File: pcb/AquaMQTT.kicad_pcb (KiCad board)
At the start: 2 copper layers, 70 x 65 mm, 22 parts, among them J1 DHW MAIN, J2 DHW HMI, J3 LLC 5V, J4 LLC 3V3, J5 Serial, J6 RTC DS3231, J7 Passthrough, Q1 BC547, Q2 BC547, Q3 BC547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

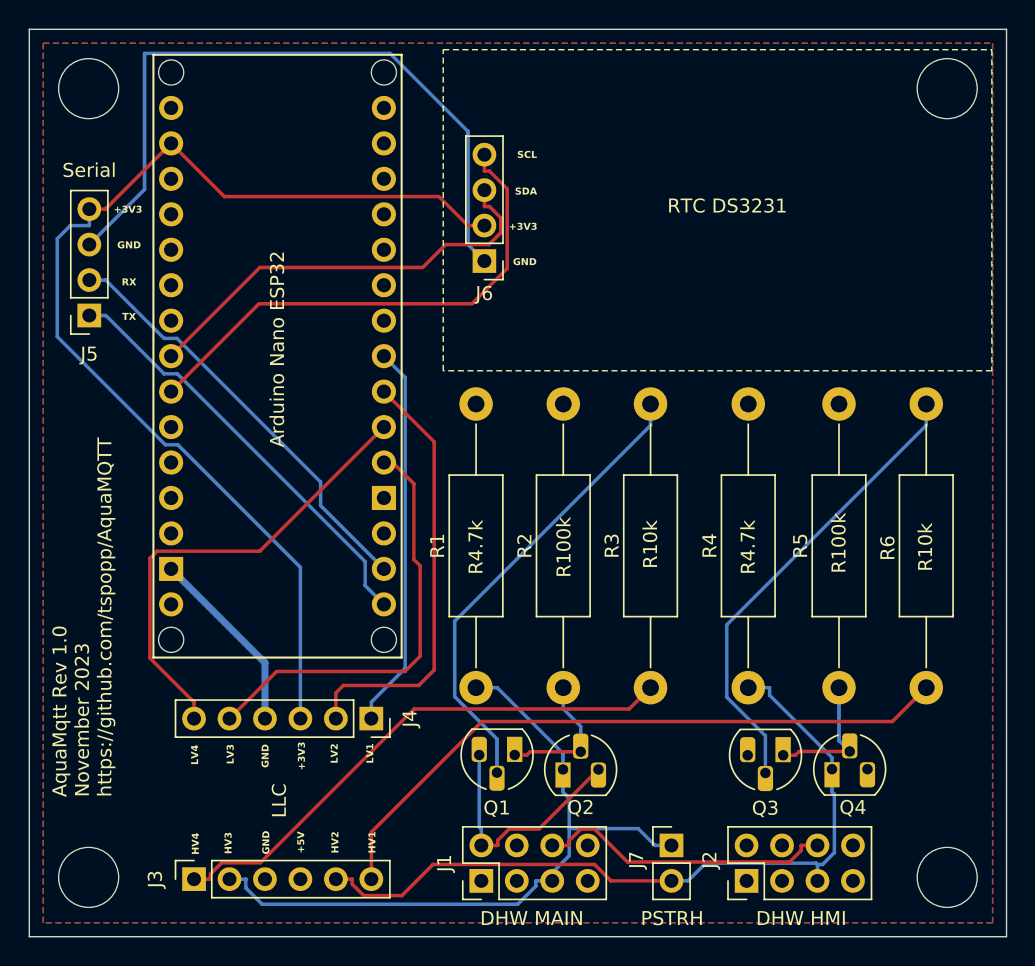
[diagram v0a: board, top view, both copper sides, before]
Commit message: feat(pcb): added pcb in rev 2.0 (rast, pre-assembly, sn74lvct45) (#72)
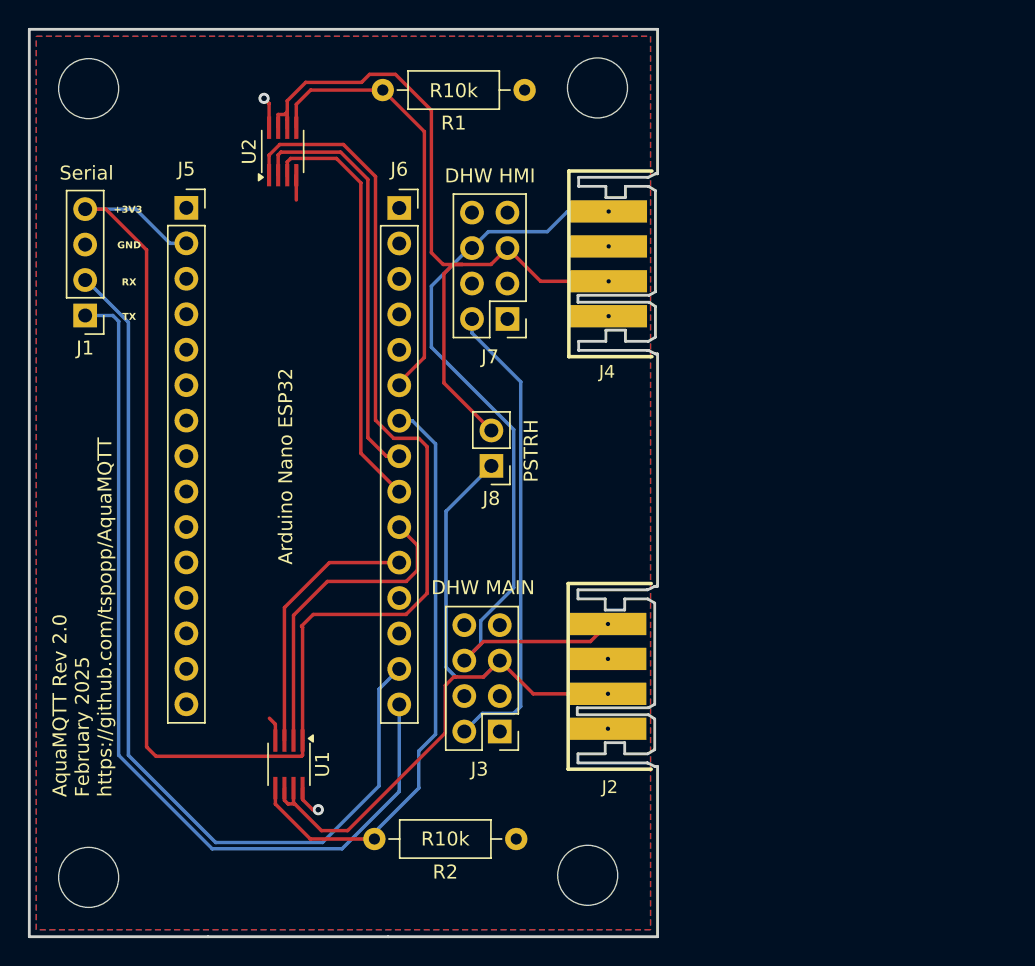
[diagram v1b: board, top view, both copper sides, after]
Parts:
- removed A2: Arduino Nano ESP32, PCM_arduino-library:Arduino_Nano_ESP32_Socket
- removed Q1, Q2, Q3, Q4: BC547, Package_TO_SOT_THT:TO-92L_HandSolder
- removed R3, R6: R10k, Resistor_THT:R_Axial_DIN0411_L9.9mm_D3.6mm_P20.32mm_Horizontal
- removed R4: R4.7k, Resistor_THT:R_Axial_DIN0411_L9.9mm_D3.6mm_P20.32mm_Horizontal
- removed R5: R100k, Resistor_THT:R_Axial_DIN0411_L9.9mm_D3.6mm_P20.32mm_Horizontal
- added J8: Passthrough, Connector_PinHeader_2.54mm:PinHeader_1x02_P2.54mm_Vertical, F.Cu at (170.1, 64.3)
- added U1: SN74LVC2T45DCUR, Package_SO:SSOP-8_2.95x2.8mm_P0.65mm, F.Cu at (155.6, 85.7)
- added U2: SN74LVC2T45DCUR, Package_SO:SSOP-8_2.95x2.8mm_P0.65mm, F.Cu at (155.2, 41.8)
- J1: value DHW MAIN -> Serial; footprint Connector_PinHeader_2.54mm:PinHeader_2x04_P2.54mm_Vertical -> Connector_PinHeader_2.54mm:PinHeader_1x04_P2.54mm_Vertical
- J2: value DHW HMI -> RAST MAIN; footprint Connector_PinHeader_2.54mm:PinHeader_2x04_P2.54mm_Vertical -> rast:RAST_3517-06_(2.5MM)_2 COPY
- J3: value LLC 5V -> DHW MAIN; footprint Connector_PinSocket_2.54mm:PinSocket_1x06_P2.54mm_Vertical -> Connector_PinHeader_2.54mm:PinHeader_2x04_P2.54mm_Vertical
- J4: value LLC 3V3 -> RAST HMI; footprint Connector_PinSocket_2.54mm:PinSocket_1x06_P2.54mm_Vertical -> rast:RAST_3517-06_(2.5MM)_2 COPY
- J5: value Serial -> Nano L; footprint Connector_PinSocket_2.54mm:PinSocket_1x04_P2.54mm_Vertical -> Connector_PinSocket_2.54mm:PinSocket_1x15_P2.54mm_Vertical
- J6: value RTC DS3231 -> Nano R; footprint Connector_PinHeader_2.54mm:PinHeader_1x04_P2.54mm_Vertical -> Connector_PinSocket_2.54mm:PinSocket_1x15_P2.54mm_Vertical
- J7: value Passthrough -> DHW HMI; footprint Connector_PinHeader_2.54mm:PinHeader_1x02_P2.54mm_Vertical -> Connector_PinHeader_2.54mm:PinHeader_2x04_P2.54mm_Vertical
- R1: value R4.7k -> R10k; footprint Resistor_THT:R_Axial_DIN0411_L9.9mm_D3.6mm_P20.32mm_Horizontal -> Resistor_THT:R_Axial_DIN0207_L6.3mm_D2.5mm_P10.16mm_Horizontal
- R2: value R100k -> R10k; footprint Resistor_THT:R_Axial_DIN0411_L9.9mm_D3.6mm_P20.32mm_Horizontal -> Resistor_THT:R_Axial_DIN0207_L6.3mm_D2.5mm_P10.16mm_Horizontal
- moved J1 49.5 mm to (141.0, 53.5), turned to 180 degrees
- moved J7 39.5 mm to (171.2, 53.8), turned to 180 degrees
- moved J4 35.3 mm to (181.8, 53.5), turned to 90 degrees
- moved R2 31.3 mm to (171.9, 91.0), turned to 180 degrees
- moved H1 25.8 mm to (177.0, 93.6)
- moved H4 25.1 mm to (177.7, 37.2)
- moved J3 24.3 mm to (170.7, 83.3), turned to 180 degrees
- moved R1 22.8 mm to (172.5, 37.4), turned to 180 degrees
- moved J2 12.7 mm to (181.8, 83.1)
- moved J5 10.4 mm to (148.2, 45.8), turned to 0 degrees
- moved J6 7.19 mm to (163.5, 45.8), turned to 0 degrees
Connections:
- J1 pad 1: +5V -> /D1/RX
- J1 pad 2: GND -> /D0/RX
- J1 pad 3: unconnected-(J1-Pin_3-Pad3) -> GND
- J1 pad 4: unconnected-(J1-Pin_4-Pad4) -> +3V3
- J2 pad 1: +5V -> DHW_UNKNOWN
- J2 pad 2: GND -> +5V
- J2 pad 3: unconnected-(J2-Pin_3-Pad3) -> OWB1_5V
- J2 pad 4: unconnected-(J2-Pin_4-Pad4) -> GND
- J3 pad 1: TXD1_5V_ESP -> +5V
- J3 pad 2: OWB1_5V -> GND
- J3 pad 3: GND -> unconnected-(J3-Pin_3-Pad3)
- J3 pad 4: +5V -> unconnected-(J3-Pin_4-Pad4)
- J3 pad 5: OWB2_5V -> OWB1_5V
- J3 pad 6: TXD2_5V_ESP -> DHW_UNKNOWN
- J4 pad 1: TXD2_3V3_ESP -> DHW_UNKNOWN
- J4 pad 2: RXD2_3V3_ESP -> +5V
- J4 pad 3: +3V3 -> OWB2_5V
- J5 pad 1: Net-(A2-D1/TX) -> /D13
- J5 pad 2: Net-(A2-D0/RX) -> +3V3
- J5 pad 3: GND -> /B0
- J5 pad 4: +3V3 -> /A0
- J6 pad 1: GND -> /D12
- J6 pad 2: +3V3 -> /D11
- J6 pad 3: Net-(A2-A4/SDA) -> /D10
- J6 pad 4: Net-(A2-A5/SCL) -> /D9
- J7 pad 1: OWB1_5V -> +5V
- J7 pad 2: OWB2_5V -> GND
- R1 pad 1: +5V -> GND
- R1 pad 2: OWB1_5V -> TXD2_3V3_ENABLE
- R2 pad 1: +5V -> GND
- R2 pad 2: Net-(Q1-C) -> TXD1_3V3_ENABLE
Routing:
- net /D0/RX: track 0.00 -> 66.6 mm
- net /D1/RX: track 0.00 -> 64.5 mm
- net TXD2_5V_ESP: track 47.4 -> 0.00 mm
- net +3V3: track 78.7 -> 123.0 mm
- net GND: track 82.1 -> 38.8 mm
- net TXD1_3V3_ENABLE: track 0.00 -> 42.7 mm
- net DHW_UNKNOWN: track 21.4 -> 62.0 mm
- net TXD1_5V_ESP: track 38.6 -> 0.00 mm
- net Net-(A2-A5/SCL): track 36.8 -> 0.00 mm
- net Net-(Q3-B): track 33.5 -> 0.00 mm
- net Net-(Q1-B): track 33.5 -> 0.00 mm
- net TXD2_3V3_ENABLE: track 0.00 -> 31.4 mm
- net Net-(A2-A4/SDA): track 31.0 -> 0.00 mm
- net Net-(A2-D1/TX): track 30.7 -> 0.00 mm
- net Net-(A2-D0/RX): track 30.7 -> 0.00 mm
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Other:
- board size 70 x 65 mm -> 45 x 65 mm
- board text added: "AquaMQTT Rev 2.0 February 2025 https://github.com/tspopp/AquaMQTT"
- board text added: "Arduino Nano ESP32"
- board text removed: "AquaMqtt Rev 1.0 November 2023 https://github.com/tspopp/AquaMQTT"
- board text removed: "HV1"
- board text removed: "HV2"
- board text removed: "HV3"
- board text removed: "HV4"
- board text removed: "LLC"
- board text removed: "LV1"
- board text removed: "LV2"
- board text removed: "LV3"
- board text removed: "LV4"
- board text removed: "SCL"
- board text removed: "SDA"
